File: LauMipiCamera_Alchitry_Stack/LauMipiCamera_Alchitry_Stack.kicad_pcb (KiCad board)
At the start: 2 copper layers, 72 x 61 mm, 10 parts, among them J1 DF40C-50DP (Site A / +3V3 onl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, J2 DF40C-80DP (Bank A / Site B /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, J3 DF40C-80DP (Bank B / Site C), SW1 DIP4 RGB/HV select

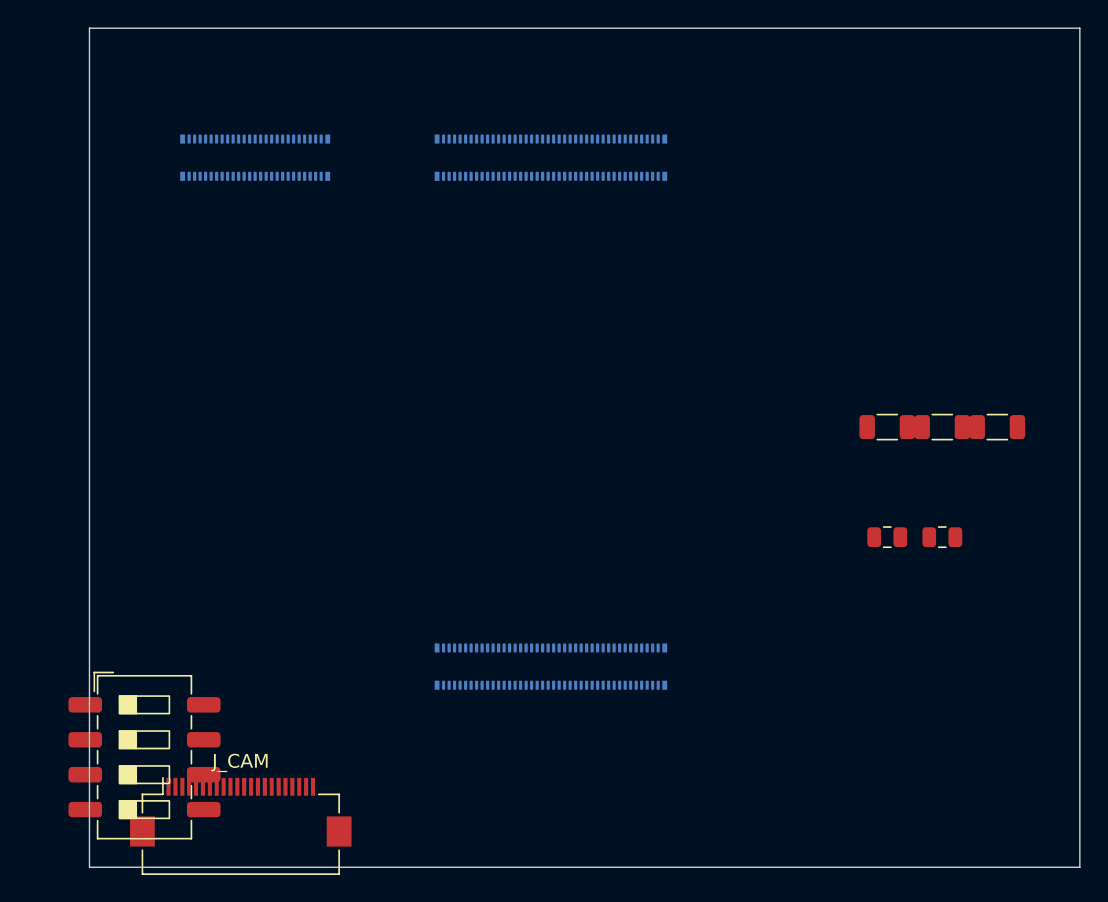
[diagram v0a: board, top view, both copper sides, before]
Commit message: hw(mipi): import netlist onto the PCB; repair what F8 broke
Update PCB from Schematic pulled all 23 nets onto the board: 268 pads netted,
0 node mismatches against the schematic netlist, and kicad-cli reports
schematic_parity: 0. The scaffold's R_1206 became R_0402 and the 9 XAPP894
front-end resistors were added. KiCad also annotated the non-numeric refs
(R_SCL -> R_SCL1, J_CAM -> J_CAM1, R_LP* -> R_LP*1); schematic and PCB agree.

F8 ran with "replace footprints", which re-created every footprint with new
UUIDs at default placement. Two consequences, both fixed here:

1. J1/J2/J3 landed on F.Cu. They are bottom-side DF40 plugs, and their old
   coordinates encoded the Alchitry stack geometry -- Site B-A = 21.5 mm in x,
   Site B-C = 37.0 mm in y (ROADMAP SS3, from Br.step). Restored all three to
   B.Cu at their original positions, injecting the freshly computed pad nets
   into the pre-F8 footprint blocks. Geometry re-verified: 21.50 / 37.00 mm.

2. Twelve clearance errors appeared, all pad-to-pad *inside* a single
   connector. Both causes are settings that were written before the nets
   existed, so nothing had ever exercised them:
     * "MipiHS clearance to other nets" (0.25 mm, ~3W) applied to pads as well
       as tracks. DF40 is 0.4 mm pitch and the FFC 0.5 mm -- those gaps are
       fixed by the connector and can never satisfy it. Scoped to
       A.Type == 'Track'; track-vs-pad is still checked.
     * The MipiHS netclass clearance floor was 0.2 mm vs the DF40's actual
       0.17 mm pad gap. Lowered to 0.15 mm; 3W routing separation still comes
       from the custom rule.

DRC now: 0 copper violations, schematic_parity 0. The 47 remaining are all
silkscreen overlaps from the auto-placement, and 112 unconnected ratsnest items
because nothing is routed.

Next: place the parts (front-end resistors belong at J3, not the FFC -- SS3.4),
then recompute the placeholder track width/gap from the real stackup.

Co-Authored-By: Claude Opus 4.8 (1M context) <nore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
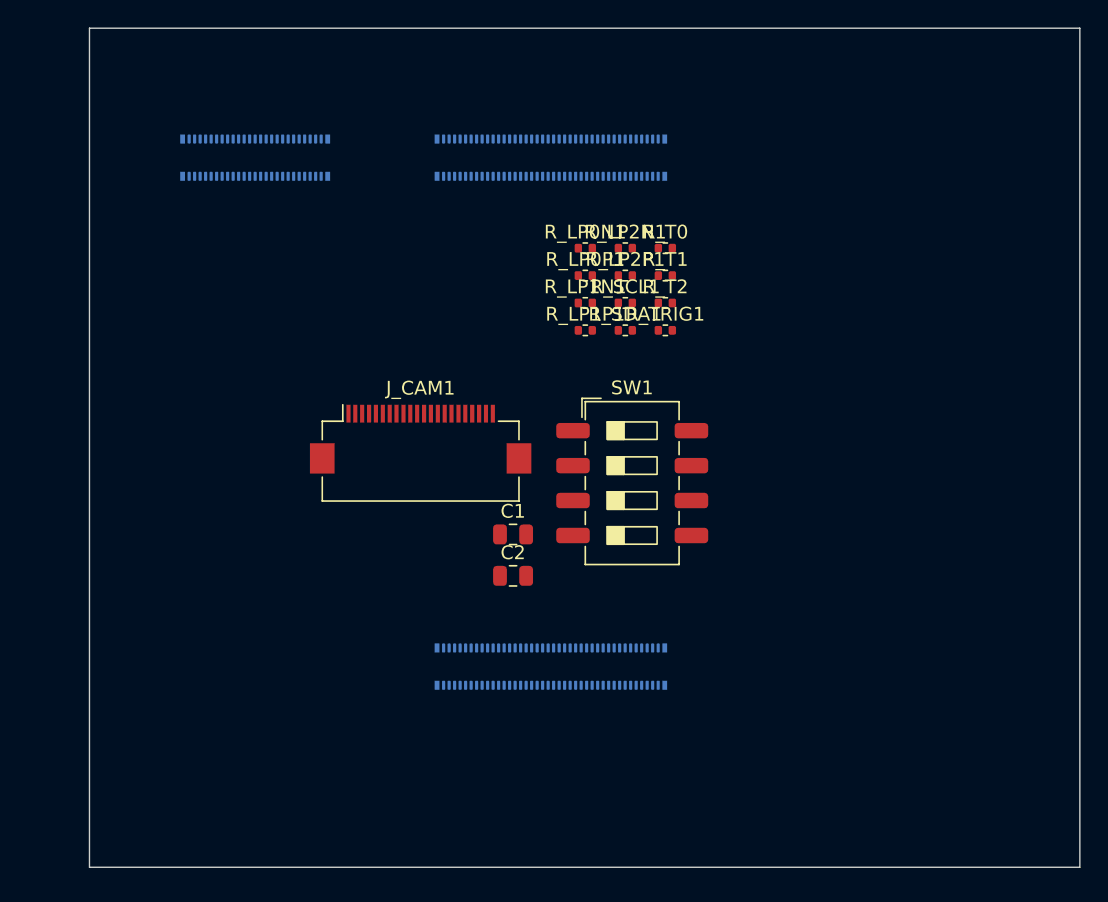
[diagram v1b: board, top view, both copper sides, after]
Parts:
- removed J_CAM: Hirose_FH12-22S-0.5SH_1x22-1MP_P0.50mm_Horizontal, Connector_FFC-FPC:Hirose_FH12-22S-0.5SH_1x22-1MP_P0.50mm_Horizontal
- removed R_SCL, R_SDA: 4k7, Resistor_SMD:R_1206_3216Metric
- removed R_TRIG: 33, Resistor_SMD:R_1206_3216Metric
- added J_CAM1: MIPI_CSI_22pin, Connector_FFC-FPC:Hirose_FH12-22S-0.5SH_1x22-1MP_P0.50mm_Horizontal, F.Cu at (148.1, 84.9)
- added R_LP0N1: 100, Resistor_SMD:R_0402_1005Metric, F.Cu at (160.0, 71.0)
- added R_LP0P1: 100, Resistor_SMD:R_0402_1005Metric, F.Cu at (160.0, 73.0)
- added R_LP1N1: 100, Resistor_SMD:R_0402_1005Metric, F.Cu at (160.0, 75.0)
- added R_LP1P1: 100, Resistor_SMD:R_0402_1005Metric, F.Cu at (160.0, 77.0)
- added R_LP2N1: 100, Resistor_SMD:R_0402_1005Metric, F.Cu at (163.0, 71.0)
- added R_LP2P1: 100, Resistor_SMD:R_0402_1005Metric, F.Cu at (163.0, 73.0)
- added R_SCL1: 4k7, Resistor_SMD:R_0402_1005Metric, F.Cu at (163.0, 75.0)
- added R_SDA1: 4k7, Resistor_SMD:R_0402_1005Metric, F.Cu at (163.0, 77.0)
- added R_T0: 150, Resistor_SMD:R_0402_1005Metric, F.Cu at (165.9, 71.0)
- added R_T1: 150, Resistor_SMD:R_0402_1005Metric, F.Cu at (165.9, 73.0)
- added R_T2: 150, Resistor_SMD:R_0402_1005Metric, F.Cu at (165.9, 75.0)
- added R_TRIG1: 33, Resistor_SMD:R_0402_1005Metric, F.Cu at (165.9, 77.0)
- C2: value 100n -> 10u
- SW1: value DIP4 RGB/HV select -> SW_DIP_x4
- moved SW1 40.7 mm to (163.5, 88.1)
- moved C2 31.3 mm to (154.8, 94.8)
- moved C1 27.2 mm to (154.8, 91.8)
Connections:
- C1 pad 1: (no net) -> +3V3
- C1 pad 2: (no net) -> GND
- C2 pad 1: (no net) -> +3V3
- C2 pad 2: (no net) -> GND
- J1 pad 1: (no net) -> +3V3
- J1 pad 10: (no net) -> unconnected-(J1-Pin_10-Pad10)
- J1 pad 11: (no net) -> +3V3
- J1 pad 12: (no net) -> unconnected-(J1-Pin_12-Pad12)
- J1 pad 13: (no net) -> unconnected-(J1-Pin_13-Pad13)
- J1 pad 14: (no net) -> unconnected-(J1-Pin_14-Pad14)
- J1 pad 15: (no net) -> unconnected-(J1-Pin_15-Pad15)
- J1 pad 16: (no net) -> unconnected-(J1-Pin_16-Pad16)
- J1 pad 17: (no net) -> unconnected-(J1-Pin_17-Pad17)
- J1 pad 18: (no net) -> unconnected-(J1-Pin_18-Pad18)
- J1 pad 19: (no net) -> unconnected-(J1-Pin_19-Pad19)
- J1 pad 2: (no net) -> unconnected-(J1-Pin_2-Pad2)
- J1 pad 20: (no net) -> unconnected-(J1-Pin_20-Pad20)
- J1 pad 21: (no net) -> unconnected-(J1-Pin_21-Pad21)
- J1 pad 22: (no net) -> unconnected-(J1-Pin_22-Pad22)
- J1 pad 23: (no net) -> unconnected-(J1-Pin_23-Pad23)
- J1 pad 24: (no net) -> unconnected-(J1-Pin_24-Pad24)
- J1 pad 25: (no net) -> unconnected-(J1-Pin_25-Pad25)
- J1 pad 26: (no net) -> unconnected-(J1-Pin_26-Pad26)
- J1 pad 27: (no net) -> unconnected-(J1-Pin_27-Pad27)
- J1 pad 28: (no net) -> unconnected-(J1-Pin_28-Pad28)
- J1 pad 29: (no net) -> unconnected-(J1-Pin_29-Pad29)
- J1 pad 3: (no net) -> +3V3
- J1 pad 30: (no net) -> unconnected-(J1-Pin_30-Pad30)
- J1 pad 31: (no net) -> unconnected-(J1-Pin_31-Pad31)
- J1 pad 32: (no net) -> unconnected-(J1-Pin_32-Pad32)
- J1 pad 33: (no net) -> unconnected-(J1-Pin_33-Pad33)
- J1 pad 34: (no net) -> unconnected-(J1-Pin_34-Pad34)
- J1 pad 35: (no net) -> unconnected-(J1-Pin_35-Pad35)
- J1 pad 36: (no net) -> unconnected-(J1-Pin_36-Pad36)
- J1 pad 37: (no net) -> unconnected-(J1-Pin_37-Pad37)
- J1 pad 38: (no net) -> unconnected-(J1-Pin_38-Pad38)
- J1 pad 39: (no net) -> unconnected-(J1-Pin_39-Pad39)
- J1 pad 4: (no net) -> unconnected-(J1-Pin_4-Pad4)
- J1 pad 40: (no net) -> unconnected-(J1-Pin_40-Pad40)
- J1 pad 41: (no net) -> unconnected-(J1-Pin_41-Pad41)
- J1 pad 42: (no net) -> unconnected-(J1-Pin_42-Pad42)
- J1 pad 43: (no net) -> unconnected-(J1-Pin_43-Pad43)
- J1 pad 44: (no net) -> unconnected-(J1-Pin_44-Pad44)
- J1 pad 45: (no net) -> unconnected-(J1-Pin_45-Pad45)
- J1 pad 46: (no net) -> unconnected-(J1-Pin_46-Pad46)
- J1 pad 47: (no net) -> unconnected-(J1-Pin_47-Pad47)
- J1 pad 48: (no net) -> unconnected-(J1-Pin_48-Pad48)
- J1 pad 49: (no net) -> unconnected-(J1-Pin_49-Pad49)
- J1 pad 5: (no net) -> +3V3
- J1 pad 50: (no net) -> unconnected-(J1-Pin_50-Pad50)
- J1 pad 6: (no net) -> unconnected-(J1-Pin_6-Pad6)
- J1 pad 7: (no net) -> unconnected-(J1-Pin_7-Pad7)
- J1 pad 8: (no net) -> unconnected-(J1-Pin_8-Pad8)
- J1 pad 9: (no net) -> +3V3
- J2 pad 1: (no net) -> GND
- J2 pad 10: (no net) -> unconnected-(J2-Pin_10-Pad10)
- J2 pad 11: (no net) -> unconnected-(J2-Pin_11-Pad11)
- J2 pad 12: (no net) -> unconnected-(J2-Pin_12-Pad12)
- J2 pad 13: (no net) -> GND
- J2 pad 14: (no net) -> GND
- J2 pad 15: (no net) -> unconnected-(J2-Pin_15-Pad15)
- J2 pad 16: (no net) -> unconnected-(J2-Pin_16-Pad16)
- J2 pad 17: (no net) -> unconnected-(J2-Pin_17-Pad17)
- J2 pad 18: (no net) -> unconnected-(J2-Pin_18-Pad18)
- J2 pad 19: (no net) -> GND
- J2 pad 2: (no net) -> GND
- J2 pad 20: (no net) -> GND
- J2 pad 21: (no net) -> unconnected-(J2-Pin_21-Pad21)
- J2 pad 22: (no net) -> unconnected-(J2-Pin_22-Pad22)
- J2 pad 23: (no net) -> unconnected-(J2-Pin_23-Pad23)
- J2 pad 24: (no net) -> unconnected-(J2-Pin_24-Pad24)
- J2 pad 25: (no net) -> GND
- J2 pad 26: (no net) -> GND
- J2 pad 27: (no net) -> unconnected-(J2-Pin_27-Pad27)
- J2 pad 28: (no net) -> unconnected-(J2-Pin_28-Pad28)
- J2 pad 29: (no net) -> unconnected-(J2-Pin_29-Pad29)
- J2 pad 3: (no net) -> unconnected-(J2-Pin_3-Pad3)
- J2 pad 30: (no net) -> unconnected-(J2-Pin_30-Pad30)
- J2 pad 31: (no net) -> GND
- J2 pad 32: (no net) -> GND
- J2 pad 33: (no net) -> unconnected-(J2-Pin_33-Pad33)
- J2 pad 34: (no net) -> unconnected-(J2-Pin_34-Pad34)
- J2 pad 35: (no net) -> unconnected-(J2-Pin_35-Pad35)
- J2 pad 36: (no net) -> unconnected-(J2-Pin_36-Pad36)
- J2 pad 37: (no net) -> GND
- J2 pad 38: (no net) -> GND
- J2 pad 39: (no net) -> unconnected-(J2-Pin_39-Pad39)
- J2 pad 4: (no net) -> unconnected-(J2-Pin_4-Pad4)
- J2 pad 40: (no net) -> unconnected-(J2-Pin_40-Pad40)
- J2 pad 41: (no net) -> unconnected-(J2-Pin_41-Pad41)
- J2 pad 42: (no net) -> unconnected-(J2-Pin_42-Pad42)
- J2 pad 43: (no net) -> GND
- J2 pad 44: (no net) -> GND
- J2 pad 45: (no net) -> unconnected-(J2-Pin_45-Pad45)
- J2 pad 46: (no net) -> unconnected-(J2-Pin_46-Pad46)
- J2 pad 47: (no net) -> unconnected-(J2-Pin_47-Pad47)
- J2 pad 48: (no net) -> unconnected-(J2-Pin_48-Pad48)
- J2 pad 49: (no net) -> GND
- J2 pad 5: (no net) -> unconnected-(J2-Pin_5-Pad5)
- J2 pad 50: (no net) -> GND
- J2 pad 51: (no net) -> unconnected-(J2-Pin_51-Pad51)
- J2 pad 52: (no net) -> unconnected-(J2-Pin_52-Pad52)
- J2 pad 53: (no net) -> unconnected-(J2-Pin_53-Pad53)
- J2 pad 54: (no net) -> unconnected-(J2-Pin_54-Pad54)
- J2 pad 55: (no net) -> GND
- J2 pad 56: (no net) -> GND
- J2 pad 57: (no net) -> unconnected-(J2-Pin_57-Pad57)
- J2 pad 58: (no net) -> unconnected-(J2-Pin_58-Pad58)
- J2 pad 59: (no net) -> unconnected-(J2-Pin_59-Pad59)
- J2 pad 6: (no net) -> unconnected-(J2-Pin_6-Pad6)
- J2 pad 60: (no net) -> unconnected-(J2-Pin_60-Pad60)
- J2 pad 61: (no net) -> GND
- J2 pad 62: (no net) -> GND
- J2 pad 63: (no net) -> unconnected-(J2-Pin_63-Pad63)
- J2 pad 64: (no net) -> unconnected-(J2-Pin_64-Pad64)
- J2 pad 65: (no net) -> unconnected-(J2-Pin_65-Pad65)
- J2 pad 66: (no net) -> unconnected-(J2-Pin_66-Pad66)
- J2 pad 67: (no net) -> GND
- J2 pad 68: (no net) -> GND
- J2 pad 69: (no net) -> unconnected-(J2-Pin_69-Pad69)
- J2 pad 7: (no net) -> GND
- J2 pad 70: (no net) -> unconnected-(J2-Pin_70-Pad70)
- J2 pad 71: (no net) -> unconnected-(J2-Pin_71-Pad71)
- J2 pad 72: (no net) -> unconnected-(J2-Pin_72-Pad72)
- J2 pad 73: (no net) -> GND
- J2 pad 74: (no net) -> GND
- J2 pad 75: (no net) -> unconnected-(J2-Pin_75-Pad75)
- J2 pad 76: (no net) -> unconnected-(J2-Pin_76-Pad76)
- J2 pad 77: (no net) -> unconnected-(J2-Pin_77-Pad77)
- J2 pad 78: (no net) -> unconnected-(J2-Pin_78-Pad78)
- J2 pad 79: (no net) -> GND
- J2 pad 8: (no net) -> GND
- J2 pad 80: (no net) -> GND
- J2 pad 9: (no net) -> unconnected-(J2-Pin_9-Pad9)
- J3 pad 1: (no net) -> GND
- J3 pad 10: (no net) -> unconnected-(J3-Pin_10-Pad10)
- J3 pad 11: (no net) -> unconnected-(J3-Pin_11-Pad11)
- J3 pad 12: (no net) -> unconnected-(J3-Pin_12-Pad12)
- J3 pad 13: (no net) -> GND
- J3 pad 14: (no net) -> GND
- J3 pad 15: (no net) -> unconnected-(J3-Pin_15-Pad15)
- J3 pad 16: (no net) -> unconnected-(J3-Pin_16-Pad16)
- J3 pad 17: (no net) -> CAM_TRIG
- J3 pad 18: (no net) -> CAM_STROBE
- J3 pad 19: (no net) -> GND
- J3 pad 2: (no net) -> GND
- J3 pad 20: (no net) -> GND
- J3 pad 21: (no net) -> CAM_SCL
- J3 pad 22: (no net) -> unconnected-(J3-Pin_22-Pad22)
- J3 pad 23: (no net) -> CAM_SDA
- J3 pad 24: (no net) -> unconnected-(J3-Pin_24-Pad24)
- J3 pad 25: (no net) -> GND
- J3 pad 26: (no net) -> GND
- J3 pad 27: (no net) -> SW_HVSV
- J3 pad 28: (no net) -> SW_BLUE
- J3 pad 29: (no net) -> SW_GREEN
- J3 pad 3: (no net) -> unconnected-(J3-Pin_3-Pad3)
- J3 pad 30: (no net) -> SW_RED
- J3 pad 31: (no net) -> GND
- J3 pad 32: (no net) -> GND
- J3 pad 33: (no net) -> LP_CK_P
- J3 pad 34: (no net) -> LP_D0_P
- J3 pad 35: (no net) -> LP_CK_N
- J3 pad 36: (no net) -> LP_D0_N
- J3 pad 37: (no net) -> GND
- J3 pad 38: (no net) -> GND
- J3 pad 39: (no net) -> unconnected-(J3-Pin_39-Pad39)
- J3 pad 4: (no net) -> unconnected-(J3-Pin_4-Pad4)
- J3 pad 40: (no net) -> CAM_D0_N
- J3 pad 41: (no net) -> unconnected-(J3-Pin_41-Pad41)
- J3 pad 42: (no net) -> CAM_D0_P
- J3 pad 43: (no net) -> GND
- J3 pad 44: (no net) -> GND
- J3 pad 45: (no net) -> CAM_CK_N
- J3 pad 46: (no net) -> CAM_D1_N
- J3 pad 47: (no net) -> CAM_CK_P
- J3 pad 48: (no net) -> CAM_D1_P
- J3 pad 49: (no net) -> GND
- J3 pad 5: (no net) -> unconnected-(J3-Pin_5-Pad5)
- J3 pad 50: (no net) -> GND
- J3 pad 51: (no net) -> LP_D1_P
- J3 pad 52: (no net) -> unconnected-(J3-Pin_52-Pad52)
- J3 pad 53: (no net) -> LP_D1_N
- J3 pad 54: (no net) -> unconnected-(J3-Pin_54-Pad54)
- J3 pad 55: (no net) -> GND
- J3 pad 56: (no net) -> GND
- J3 pad 57: (no net) -> unconnected-(J3-Pin_57-Pad57)
- J3 pad 58: (no net) -> unconnected-(J3-Pin_58-Pad58)
- J3 pad 59: (no net) -> unconnected-(J3-Pin_59-Pad59)
- J3 pad 6: (no net) -> unconnected-(J3-Pin_6-Pad6)
- J3 pad 60: (no net) -> unconnected-(J3-Pin_60-Pad60)
- J3 pad 61: (no net) -> GND
- J3 pad 62: (no net) -> GND
- J3 pad 63: (no net) -> unconnected-(J3-Pin_63-Pad63)
- J3 pad 64: (no net) -> unconnected-(J3-Pin_64-Pad64)
- J3 pad 65: (no net) -> unconnected-(J3-Pin_65-Pad65)
- J3 pad 66: (no net) -> unconnected-(J3-Pin_66-Pad66)
- J3 pad 67: (no net) -> GND
- J3 pad 68: (no net) -> GND
- J3 pad 69: (no net) -> unconnected-(J3-Pin_69-Pad69)
- J3 pad 7: (no net) -> GND
- J3 pad 70: (no net) -> unconnected-(J3-Pin_70-Pad70)
- J3 pad 71: (no net) -> unconnected-(J3-Pin_71-Pad71)
- J3 pad 72: (no net) -> unconnected-(J3-Pin_72-Pad72)
- J3 pad 73: (no net) -> GND
- J3 pad 74: (no net) -> GND
- J3 pad 75: (no net) -> unconnected-(J3-Pin_75-Pad75)
- J3 pad 76: (no net) -> unconnected-(J3-Pin_76-Pad76)
- J3 pad 77: (no net) -> unconnected-(J3-Pin_77-Pad77)
- J3 pad 78: (no net) -> unconnected-(J3-Pin_78-Pad78)
- J3 pad 79: (no net) -> GND
- J3 pad 8: (no net) -> GND
- J3 pad 80: (no net) -> GND
- J3 pad 9: (no net) -> unconnected-(J3-Pin_9-Pad9)
- SW1 pad 1: (no net) -> SW_HVSV
- SW1 pad 2: (no net) -> SW_BLUE
- SW1 pad 3: (no net) -> SW_GREEN
- SW1 pad 4: (no net) -> SW_RED
- SW1 pad 5: (no net) -> GND
- SW1 pad 6: (no net) -> GND
- SW1 pad 7: (no net) -> GND
- SW1 pad 8: (no net) -> GND

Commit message: hw(mipi): adopt the trigger board's real outline (55x45 mm) for the MIPI board
The scaffold shipped a placeholder 72x61 mm rectangle. Replace it with the
Edge.Cuts geometry of LauCameraTrigger_Alchitry_Stack, which is fabricated and
known to mate the Alchitry stack:

  * 55 x 45 mm body, 1.5 mm chamfered corners
  * right-edge relief notch (x 169.045..174.545, y 68.412..97.412)
  * 4x mounting holes, dia 2.2 mm, 50 x 40 mm centres

Copied verbatim with ZERO translation: both boards already place the three DF40
sites at identical coordinates (J1 136.045,64.413 / J2 157.545,64.413 /
J3 157.545,101.413). Cross-checks against ROADMAP SS3 (from Br.step): the outline
sits -38.0 mm in x and +4.0 mm in y relative to J3, exactly the Site C offset,
and the site spacing is 21.5 / 37.0 mm.

Shrinking the board left SW1 hanging over the notch (4 copper_edge_clearance
errors). Moved it to the free lower-left area at (132,93) -- a holding position,
not a considered placement. An intermediate try at x=160 collided with C1, so
the move was checked against every footprint's pad extents.

DRC: 0 copper violations, schematic_parity 0. The 47 remaining are silkscreen
overlaps from the auto-placement; 112 ratsnest items since nothing is routed.

Open: confirm the notch is a stack clearance rather than trigger-board specific.

Co-Authored-By: Claude Opus 4.8 (1M context) <noreply@anthropic.com>
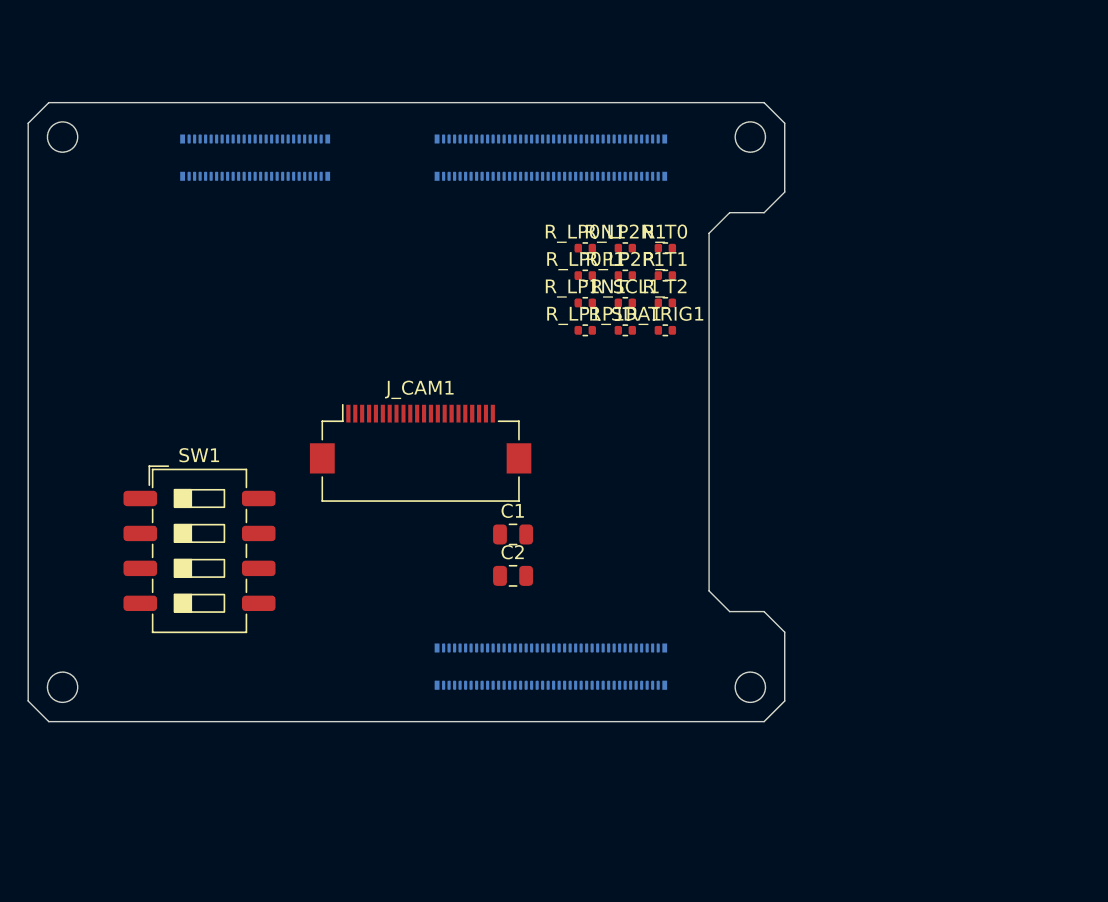
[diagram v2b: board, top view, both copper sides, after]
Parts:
- moved SW1 31.8 mm to (132.0, 93.0)
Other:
- board size 72 x 61 mm -> 55 x 45 mm
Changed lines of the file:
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@@
 	(footprint "Button_Switch_SMD:SW_DIP_SPSTx04_Slide_6.7x11.72mm_W8.61mm_P2.54mm_LowProfile"
 		(layer "F.Cu")
-		(at 163.455 88.07)
+		(at 132.00 93.00)
 		(descr "SMD 4x-dip-switch SPST , Slide, row spacing 8.61 mm (338 mils), body size 6.7x11.72mm (see e.g. https://www.ctscorp.com/wp-content/uploads/219.pdf), SMD, LowProfile")
 		(tags "SMD DIP Switch SPST Slide 8.61mm 338mil SMD LowProfile")
@@
 	)
 	(gr_line
-		(start 124 55)
-		(end 196 55)
-		(stroke
-			(width 0.1)
-			(type solid)
-		)
-		(layer "Edge.Cuts")
-	)
-	(gr_line
-		(start 124 116)
-		(end 124 55)
-		(stroke
-			(width 0.1)
-			(type solid)
-		)
-		(layer "Edge.Cuts")
-	)
-	(gr_line
-		(start 196 55)
-		(end 196 116)
-		(stroke
-			(width 0.1)
-			(type solid)
-		)
-		(layer "Edge.Cuts")
-	)
-	(gr_line
-		(start 196 116)
-		(end 124 116)
-		(stroke
-			(width 0.1)
-			(type solid)
-		)
-		(layer "Edge.Cuts")
+		(start 119.545 61.912)
+		(end 119.545 103.912)
+		(stroke
+			(width 0.1)
+			(type default)
+		)
+		(layer "Edge.Cuts")
+	)
+	(gr_line
+		(start 119.545 103.912)
+		(end 121.045 105.412)
+		(stroke
+			(width 0.1)
+			(type default)
+		)
+		(layer "Edge.Cuts")
+	)
+	(gr_line
+		(start 121.045 60.412)
+		(end 119.545 61.912)
+		(stroke
+			(width 0.1)
+			(type default)
+		)
+		(layer "Edge.Cuts")
+	)
+	(gr_line
+		(start 121.045 105.412)
+		(end 173.045 105.412)
+		(stroke
+			(width 0.1)
+			(type default)
+		)
+		(layer "Edge.Cuts")
+	)
+	(gr_circle
+		(center 122.045 62.912)
+		(end 123.145 62.912)
+		(stroke
+			(width 0.1)
+			(type default)
+		)
+		(fill no)
+		(layer "Edge.Cuts")
+	)
+	(gr_circle
+		(center 122.045 102.912)
+		(end 123.145 102.912)
+		(stroke
+			(width 0.1)
+			(type default)
+		)
+		(fill no)
+		(layer "Edge.Cuts")
+	)
+	(gr_line
+		(start 169.045 69.912)
+		(end 170.545 68.412)
+		(stroke
+			(width 0.1)
+			(type default)
+		)
+		(layer "Edge.Cuts")
+	)
+	(gr_line
+		(start 169.045 95.912)
+		(end 169.045 69.912)
+		(stroke
+			(width 0.1)
+			(type default)
+		)
+		(layer "Edge.Cuts")
+	)
+	(gr_line
+		(start 170.545 68.412)
+		(end 173.045 68.412)
+		(stroke
+			(width 0.1)
+			(type default)
+		)
+		(layer "Edge.Cuts")
+	)
+	(gr_line
+		(start 170.545 97.412)
+		(end 169.045 95.912)
+		(stroke
+			(width 0.1)
+			(type default)
+		)
+		(layer "Edge.Cuts")
+	)
+	(gr_circle
+		(center 172.045 62.912)
+		(end 173.145 62.912)
+		(stroke
+			(width 0.1)
+			(type default)
+		)
+		(fill no)
+		(layer "Edge.Cuts")
+	)
+	(gr_circle
+		(center 172.045 102.912)
+		(end 173.145 102.912)
+		(stroke
+			(width 0.1)
+			(type default)
+		)
+		(fill no)
+		(layer "Edge.Cuts")
+	)
+	(gr_line
+		(start 173.045 60.412)
+		(end 121.045 60.412)
+		(stroke
+			(width 0.1)
+			(type default)
+		)
+		(layer "Edge.Cuts")
+	)
+	(gr_line
+		(start 173.045 68.412)
+		(end 174.545 66.912)
+		(stroke
+			(width 0.1)
+			(type default)
+		)
+		(layer "Edge.Cuts")
+	)
+	(gr_line
+		(start 173.045 97.412)
+		(end 170.545 97.412)
+		(stroke
+			(width 0.1)
+			(type default)
+		)
+		(layer "Edge.Cuts")
+	)
+	(gr_line
+		(start 173.045 105.412)
+		(end 174.545 103.912)
+		(stroke
+			(width 0.1)
+			(type default)
+		)
+		(layer "Edge.Cuts")
+	)
+	(gr_line
+		(start 174.545 61.912)
+		(end 173.045 60.412)
+		(stroke
+			(width 0.1)
+			(type default)
+		)
+		(layer "Edge.Cuts")
+	)
+	(gr_line
+		(start 174.545 66.912)
+		(end 174.545 61.912)
+		(stroke
+			(width 0.1)
+			(type default)
+		)
+		(layer "Edge.Cuts")
+	)
+	(gr_line
+		(start 174.545 98.912)
+		(end 173.045 97.412)
+		(stroke
+			(width 0.1)
+			(type default)
+		)
+		(layer "Edge.Cuts")
+	)
+	(gr_line
+		(start 174.545 103.912)
+		(end 174.545 98.912)
+		(stroke
+			(width 0.1)
+			(type default)
+		)
+		(layer "Edge.Cuts")
